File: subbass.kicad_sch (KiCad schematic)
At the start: 10 parts, among them U1 OPA1656ID

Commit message: preparando fase subsonica
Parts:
- added R5: 2k, symbol Device:R
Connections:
- net GND: now also R5.1
- net VOUT_SUB: now reaches C4.2, U1.1, U1.2 (-)
- net VOUT_SUB: now also R5.2
- net VIN_SUB: now reaches R3.1, V3.1
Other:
- moved on the sheet: U1B

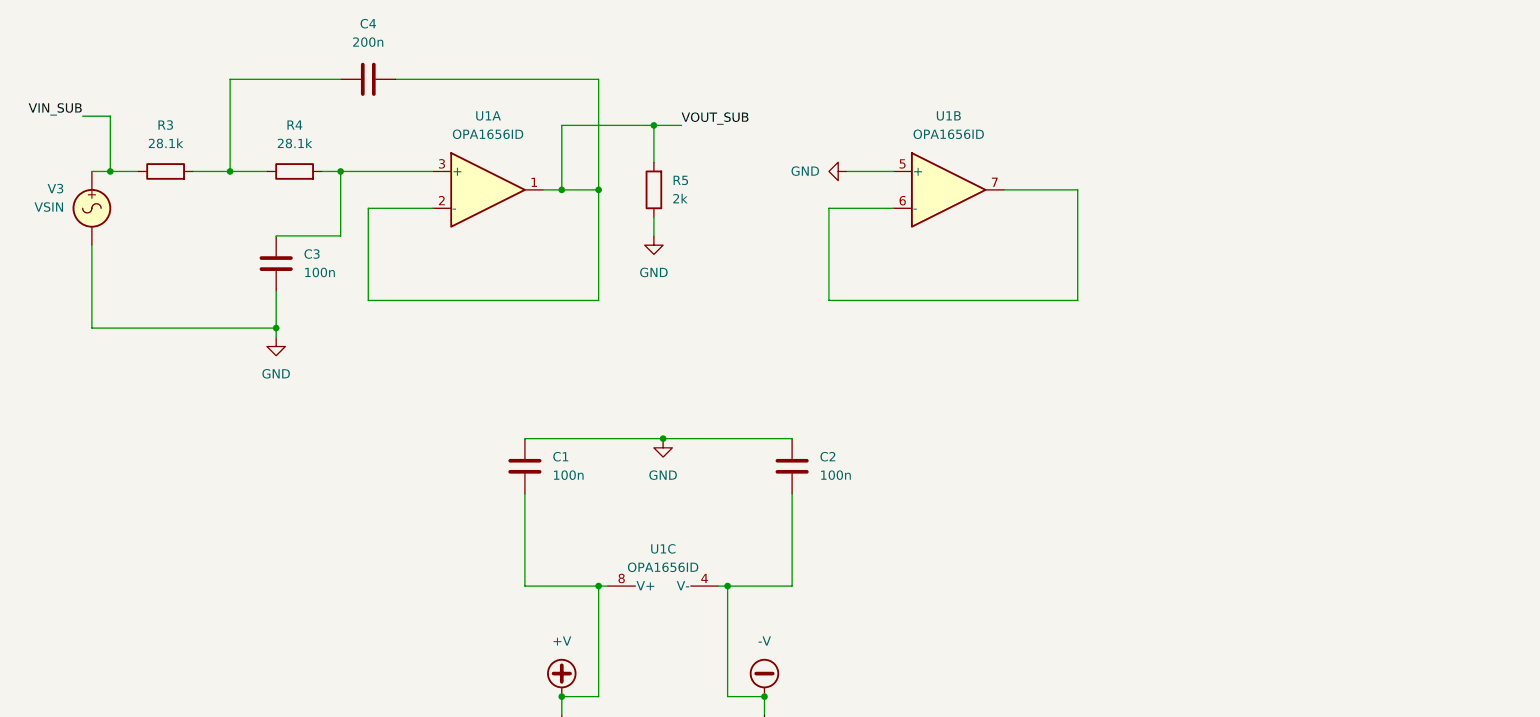
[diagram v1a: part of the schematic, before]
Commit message: Valida cascata subbass 40 Hz e subsonico 10 Hz em ±15 V
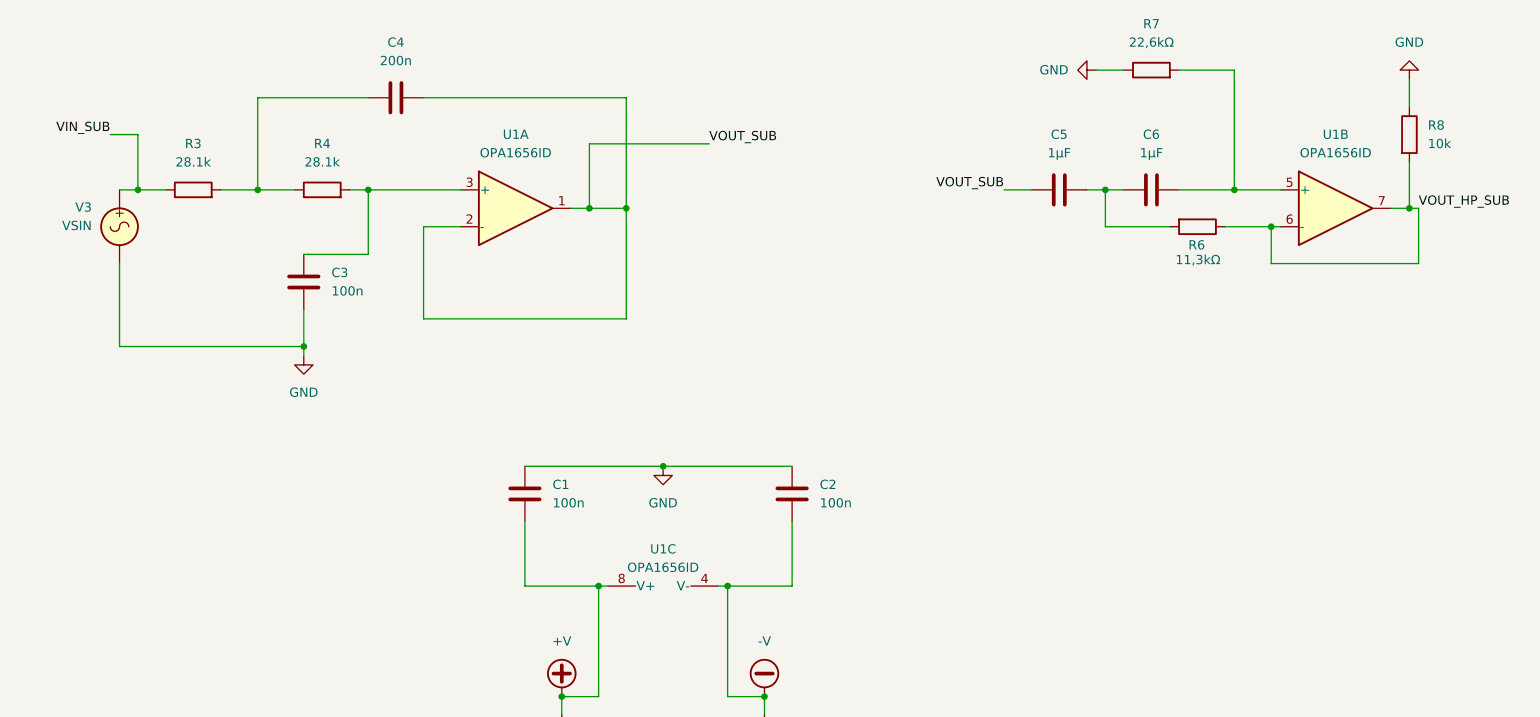
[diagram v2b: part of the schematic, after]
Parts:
- removed R5: 2k, symbol Device:R
- added C5, C6: 1µF, symbol Device:C
- added R6: 11,3kΩ, symbol Device:R
- added R7: 22,6kΩ, symbol Device:R
- added R8: 10k, symbol Device:R
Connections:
- net GND: now also R7.1, R8.1; no longer U1.5 (+)
- net VOUT_SUB: now also C5.1
- net VOUT_HP_SUB: now reaches U1.6 (-), U1.7
- net VOUT_HP_SUB: now also R6.1, R8.2
- new net: C5.2, C6.1, R6.2
- new net: C6.2, R7.2, U1.5 (+)
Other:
- moved on the sheet: C1, C2, C3, C4, R3, R4, U1A, U1B, V3

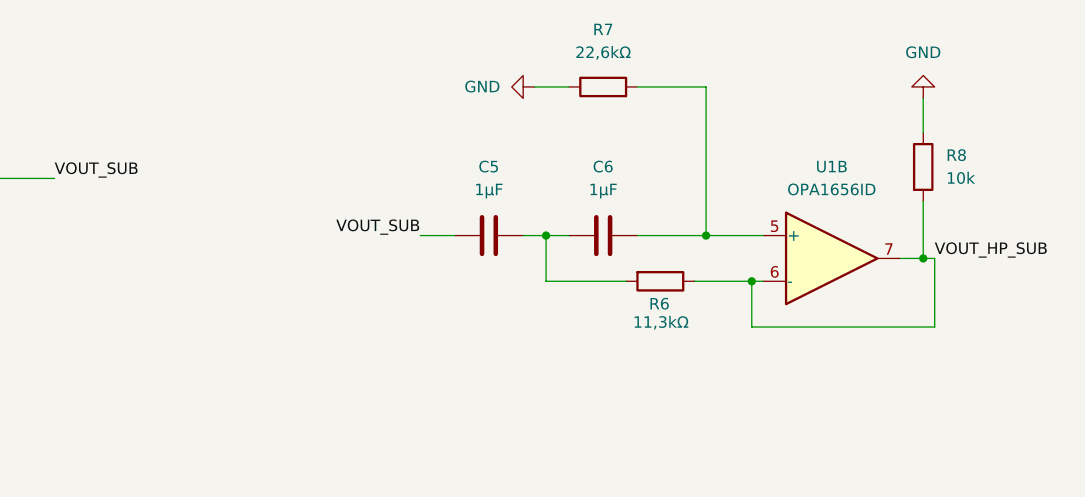
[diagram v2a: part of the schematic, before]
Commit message: Conclui ensaios de degrau e sequenciamento da alimentacao do subbass
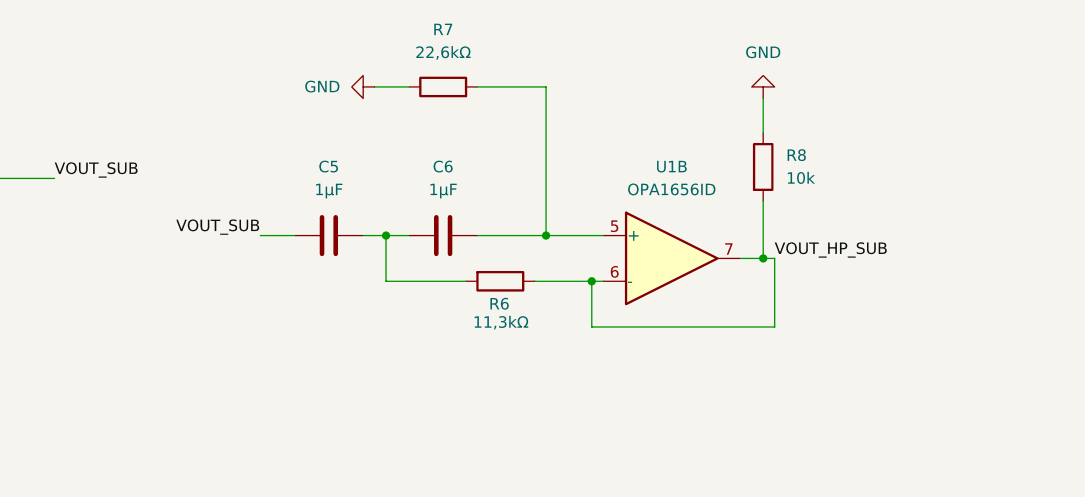
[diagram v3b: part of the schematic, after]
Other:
- moved on the sheet: C5, C6, R6, R7, R8, U1B

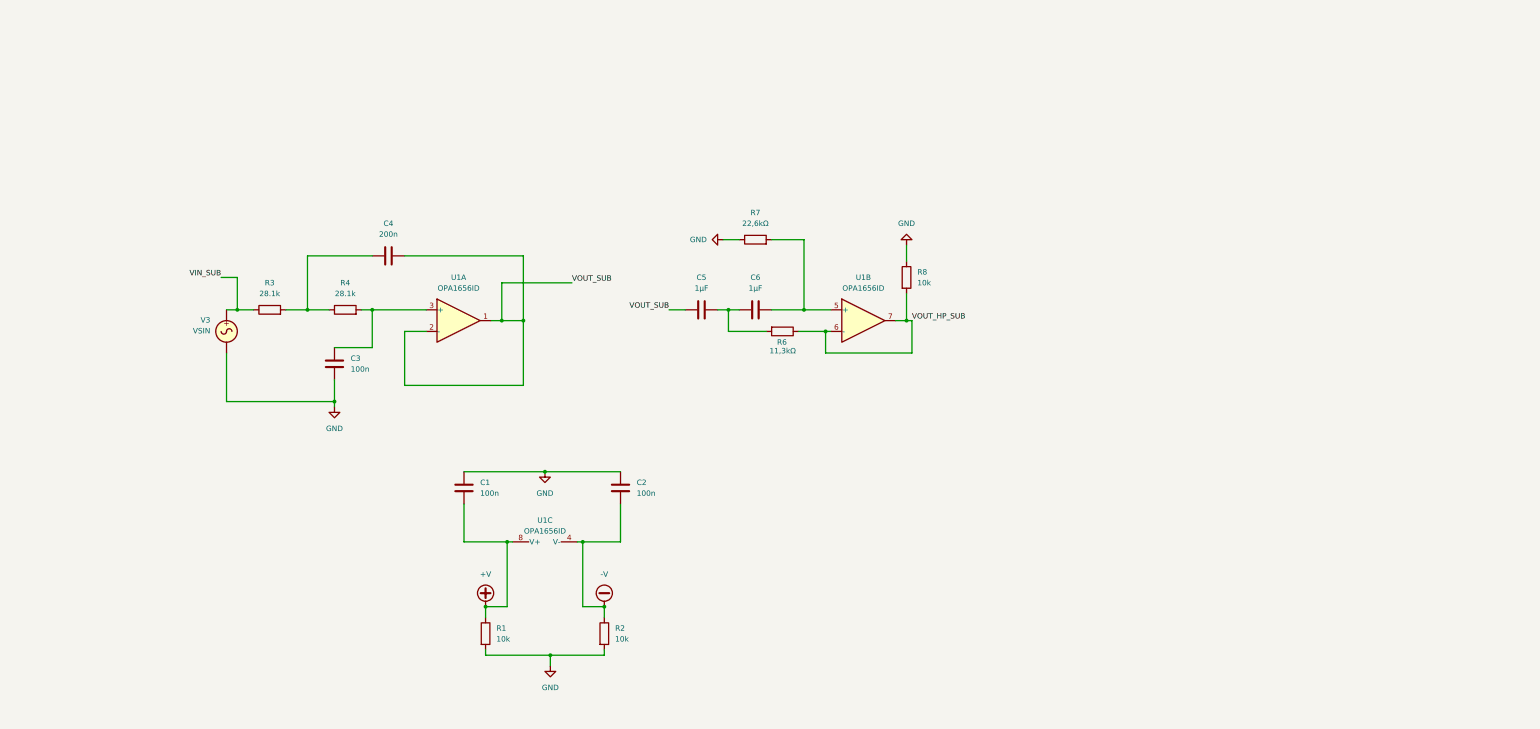
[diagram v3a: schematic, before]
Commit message: Add SubBass mute control and verification scripts
- Introduced a new SPICE subcircuit for SubBass mute control, implementing a dual-rail supervisor with diagnostic outputs.
- Created a symbol library for Hi-Fi audio components in KiCad.
- Added a Python script to plot results from SubBass simulations, visualizing startup, shutdown, and AC response.
- Developed a verification script for the SubBass design, exporting netlists and validating functionality through simulation with ngspice.
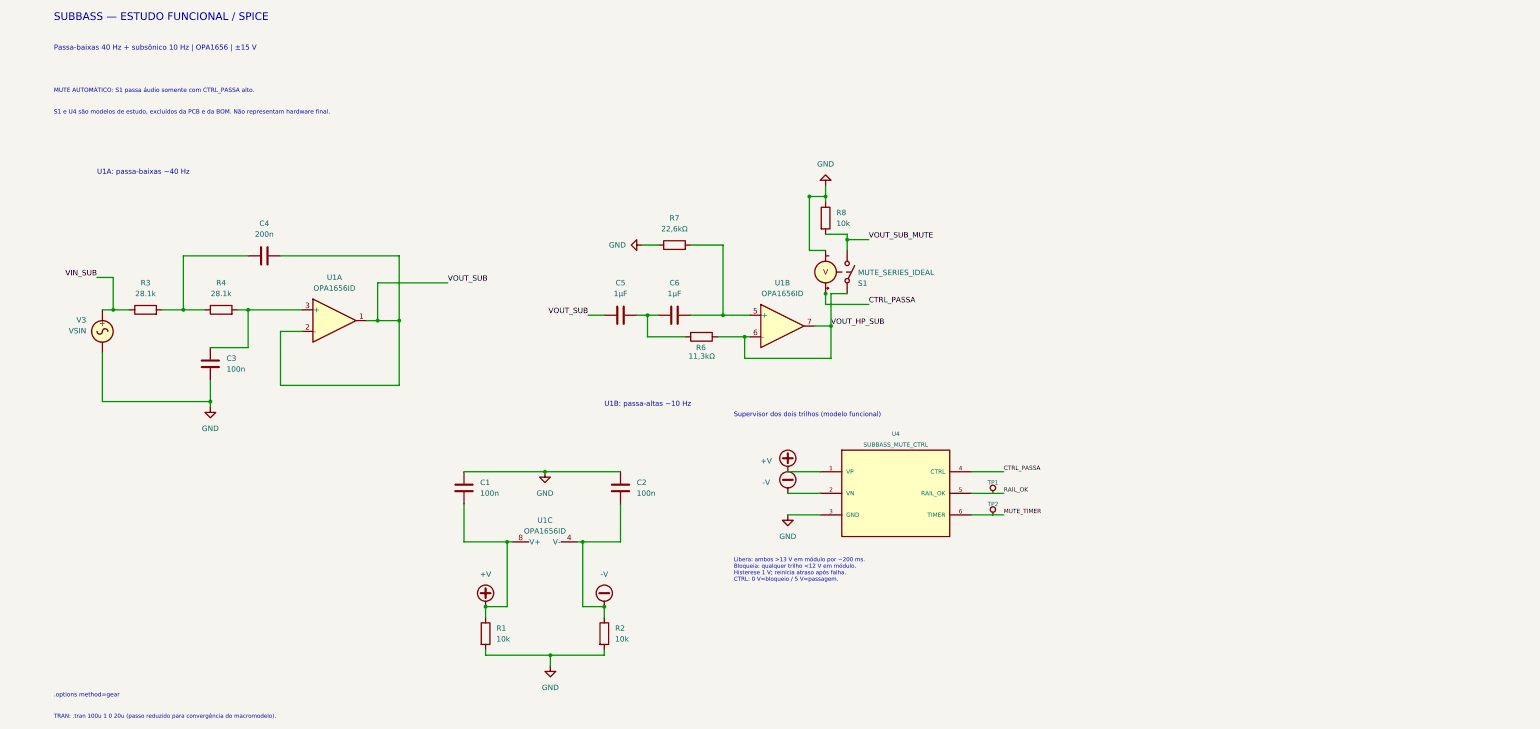
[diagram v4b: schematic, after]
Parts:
- added S1: MUTE_SERIES_IDEAL, symbol Simulation_SPICE:SWITCH
- added TP1, TP2: SIM_TESTPOINT, symbol Audio_HiFi:SIM_TESTPOINT
- added U4: SUBBASS_MUTE_CTRL, symbol Audio_HiFi:SUBBASS_MUTE_CTRL
- V3: now left out of the parts list
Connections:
- net +V: now also U4.1 (VP)
- net -V: now also U4.2 (VN)
- net GND: now also S1.4 (C-), U4.3 (GND)
- net VOUT_HP_SUB: now also S1.1 (N+); no longer R8.2
- new net CTRL_PASSA: S1.3 (C+), U4.4 (CTRL)
- new net MUTE_TIMER: TP2.1, U4.6 (TIMER)
- new net RAIL_OK: TP1.1, U4.5 (RAIL_OK)
- new net VOUT_SUB_MUTE: R8.2, S1.2 (N-)
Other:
- note added: ".options method=gear"
- note added: "Libera: ambos >13 V em módulo por ~200 ms. Bloqueia: qualquer trilho <12 V em módulo. Histerese 1 V; reinicia atraso após falha. CTRL: 0 V=bloqueio / 5 V=passagem."
- note added: "MUTE AUTOMÁTICO: S1 passa áudio somente com CTRL_PASSA alto."
- note added: "Passa-baixas 40 Hz + subsônico 10 Hz | OPA1656 | ±15 V"
- note added: "S1 e U4 são modelos de estudo, excluídos da PCB e da BOM. Não representam hardware final."
- note added: "SUBBASS — ESTUDO FUNCIONAL / SPICE"
- note added: "Supervisor dos dois trilhos (modelo funcional)"
- note added: "TRAN: .tran 100u 1 0 20u (passo reduzido para convergência do macromodelo)."
- note added: "U1A: passa-baixas ~40 Hz"
- note added: "U1B: passa-altas ~10 Hz"
- moved on the sheet: C3, C4, C5, C6, R3, R4, R6, R7, R8, U1A, U1B, V3

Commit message: Finalize SubBass mute hardware proposal
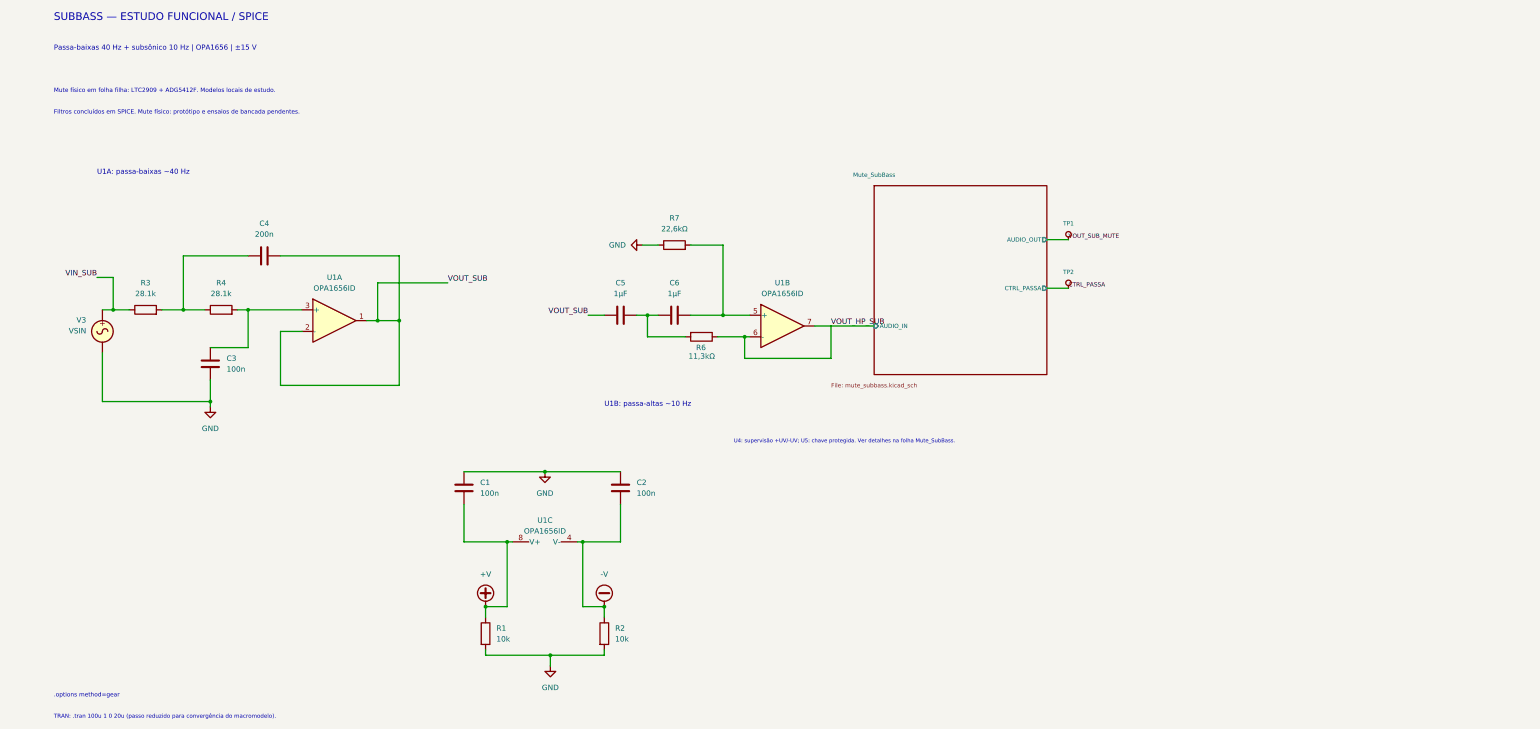
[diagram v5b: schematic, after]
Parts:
- removed R8: 10k, symbol Device:R
- removed S1: MUTE_SERIES_IDEAL, symbol Simulation_SPICE:SWITCH
- removed TP1, TP2: SIM_TESTPOINT, symbol Audio_HiFi:SIM_TESTPOINT
- removed U4: SUBBASS_MUTE_CTRL, symbol Audio_HiFi:SUBBASS_MUTE_CTRL
- added TP1, TP2: TestPoint, TestPoint:TestPoint_Pad_D1.5mm, symbol Audio_HiFi:TESTPOINT
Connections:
- net CTRL_PASSA: now also TP2.1
- net VOUT_SUB_MUTE: now also TP1.1
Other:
- added sheet Mute_SubBass (mute_subbass.kicad_sch)
- note added: "Filtros concluídos em SPICE. Mute físico: protótipo e ensaios de bancada pendentes."
- note added: "Mute físico em folha filha: LTC2909 + ADG5412F. Modelos locais de estudo."
- note added: "U4: supervisão +UV/-UV; U5: chave protegida. Ver detalhes na folha Mute_SubBass."
- note removed: "Libera: ambos >13 V em módulo por ~200 ms. Bloqueia: qualquer trilho <12 V em módulo. Histerese 1 V; reinicia atraso após falha. CTRL: 0 V=bloqueio / 5 V=passagem."
- note removed: "MUTE AUTOMÁTICO: S1 passa áudio somente com CTRL_PASSA alto."
- note removed: "S1 e U4 são modelos de estudo, excluídos da PCB e da BOM. Não representam hardware final."
- note removed: "Supervisor dos dois trilhos (modelo funcional)"
